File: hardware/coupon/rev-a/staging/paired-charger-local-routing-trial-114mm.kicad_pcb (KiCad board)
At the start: 6 copper layers, 114 x 32.5 mm, 483 parts, among them J1 USB4505-03-0-A, J2 S2B-PH-SM4-TB, SW1 EVQP7J01P, SW2 JS202011JCQN, U1 TLC59581RTQT, U11 SN74LVC1G04DBVR, U17 SN74LVC1G11DBVR, U2 74HC4514PW,118, U23 SN74LVC1G06DBVR, U24 SN74LVC2G17DBVR, U25 SN74LVC2G17DBVR, U29 TPS70933DBVR, U3 ESP32-S3-WROOM-1U-N16R8, U31 TUSB320LAIRWBR, U32 TS3USB31ERSER, U33 TPD4E05U06DQAR, U34 TPS3808G01DBVR, U35 MAX17048G+T10, U36 TPS631000DRLR, U37 TPS63020DSJT, U38 2.5V shunt, U39 TMP390A2DRLR, U40 SN74AUP1G125DBVR, U41 BQ24074RGTR, U42 SN74AUP1G125DBVR, U43 SN74AUP1G125DBVR, U44 TPS259474ARPWR, U45 TPS259474ARPWR, U46 TCA9517ADGKR, U47 TPS3823A-33DBVR, U48 SN74LVC1G04DSFR, U49 SN74LVC1G74RSER, U50 SN74LVC1G74RSER, U51 SN74LVC1G11DRYR, U52 SN74LVC1G08DSFR, U53 TLV6700DSER, U54 SN74LVC2G00DCUR, U55 SN74LVC2G08DCUR

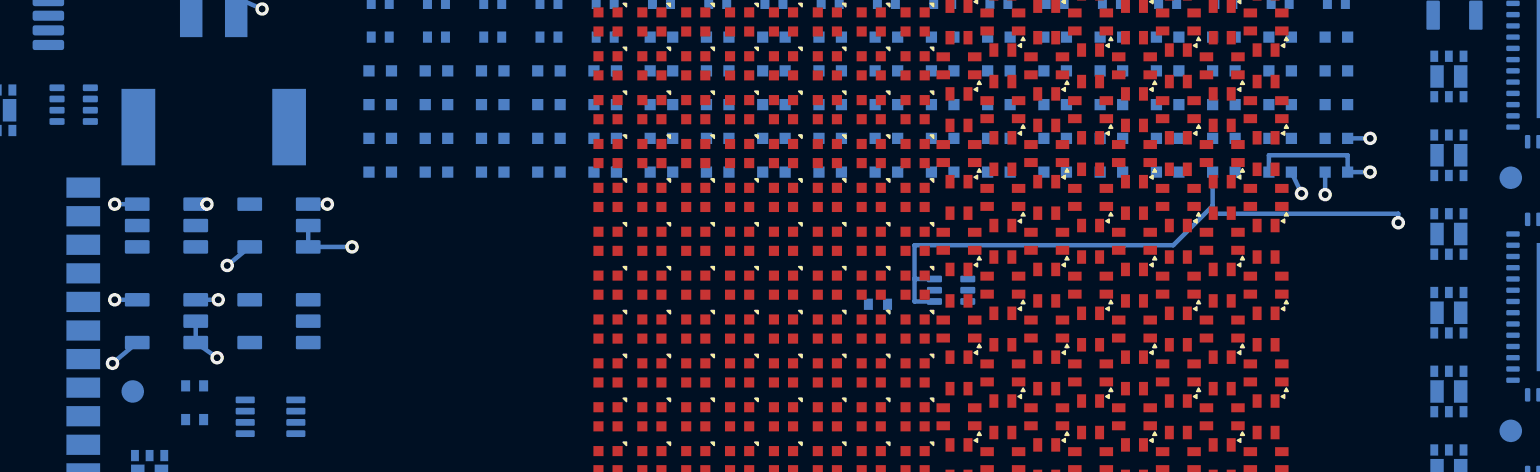
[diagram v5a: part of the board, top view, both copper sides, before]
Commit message: Join charger permission logic supply and temperature sensor returns
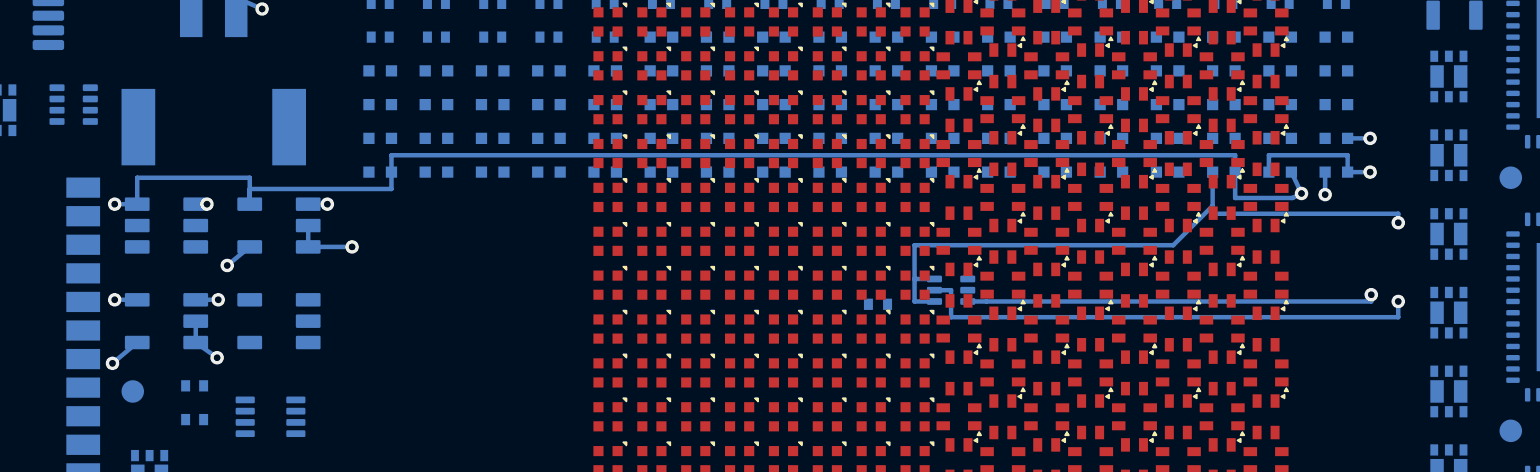
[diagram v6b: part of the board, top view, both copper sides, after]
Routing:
- net +3V3_USB: track 24.2 -> 130.5 mm, vias 6 -> 7
- net GND: track 229.2 -> 250.4 mm, vias 20 -> 21
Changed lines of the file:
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@@
+	)
+	(segment
+		(start 21.45 10.5)
+		(end 21.45 11.675)
+		(width 0.2)
+		(layer "B.Cu")
+		(net "+3V3_USB")
 	)
 	(segment
@@
 		(layer "B.Cu")
 		(net "+BAT_PROTECTED_DRAFT")
+	)
+	(segment
+		(start 26.45 10.5)
+		(end 21.45 10.5)
+		(width 0.2)
+		(layer "B.Cu")
+		(net "+3V3_USB")
+	)
+	(segment
+		(start 26.45 11)
+		(end 32.75 11)
+		(width 0.2)
+		(layer "B.Cu")
+		(net "+3V3_USB")
+	)
+	(segment
+		(start 26.45 11.675)
+		(end 26.45 10.5)
+		(width 0.2)
+		(layer "B.Cu")
+		(net "+3V3_USB")
+	)
+	(segment
+		(start 26.45 11.675)
+		(end 26.45 11)
+		(width 0.2)
+		(layer "B.Cu")
+		(net "+3V3_USB")
 	)
 	(segment
@@
 	)
 	(segment
+		(start 32.75 10.25)
+		(end 32.75 9.5)
+		(width 0.2)
+		(layer "B.Cu")
+		(net "+3V3_USB")
+	)
+	(segment
+		(start 32.75 11)
+		(end 32.75 10.25)
+		(width 0.2)
+		(layer "B.Cu")
+		(net "+3V3_USB")
+	)
+	(segment
+		(start 32.75 9.5)
+		(end 70.25 9.5)
+		(width 0.2)
+		(layer "B.Cu")
+		(net "+3V3_USB")
+	)
+	(segment
 		(start 5.3 1.4)
 		(end 6.5 1.4)
@@
 		(layer "B.Cu")
 		(net "TEMP_OK")
+	)
+	(segment
+		(start 56.885 15.5)
+		(end 57.625 15.5)
+		(width 0.2)
+		(layer "B.Cu")
+		(net "+3V3_USB")
+	)
+	(segment
+		(start 57.625 15.5)
+		(end 57.625 16.7)
+		(width 0.2)
+		(layer "B.Cu")
+		(net "+3V3_USB")
+	)
+	(segment
+		(start 57.625 16.7)
+		(end 77.5 16.7)
+		(width 0.2)
+		(layer "B.Cu")
+		(net "+3V3_USB")
+	)
+	(segment
+		(start 58.365 16)
+		(end 59.2 16)
+		(width 0.2)
+		(layer "B.Cu")
+		(net "GND")
+	)
+	(segment
+		(start 59.2 16)
+		(end 76.3 16)
+		(width 0.2)
+		(layer "B.Cu")
+		(net "GND")
 	)
 	(segment
@@
 	)
 	(segment
+		(start 70.25 10.25)
+		(end 70.25 11.4)
+		(width 0.2)
+		(layer "B.Cu")
+		(net "+3V3_USB")
+	)
+	(segment
+		(start 70.25 11.4)
+		(end 72.8 11.4)
+		(width 0.2)
+		(layer "B.Cu")
+		(net "+3V3_USB")
+	)
+	(segment
+		(start 70.25 9.5)
+		(end 70.25 10.25)
+		(width 0.2)
+		(layer "B.Cu")
+		(net "+3V3_USB")
+	)
+	(segment
 		(start 71.75 10.25)
 		(end 71.75 9.5)
@@
 	)
 	(segment
+		(start 72.8 11.4)
+		(end 73.2 11.2)
+		(width 0.2)
+		(layer "B.Cu")
+		(net "+3V3_USB")
+	)
+	(segment
 		(start 73.2 11.2)
 		(end 76.25 8.75)
@@
 	)
 	(segment
+		(start 76.25 8.75)
+		(end 91.2 6.625)
+		(width 0.2)
+		(layer "In2.Cu")
+		(net "+3V3_USB")
+	)
+	(segment
+		(start 76.3 15.7)
+		(end 76.3 18.73)
+		(width 0.2)
+		(layer "In2.Cu")
+		(net "GND")
+	)
+	(segment
+		(start 76.3 16)
+		(end 76.3 15.7)
+		(width 0.2)
+		(layer "B.Cu")
+		(net "GND")
+	)
+	(segment
 		(start 77.5 12.1)
 		(end 77.5 12.5)
@@
 	)
 	(segment
+		(start 77.5 16)
+		(end 78.5 16)
+		(width 0.2)
+		(layer "In2.Cu")
+		(net "+3V3_USB")
+	)
+	(segment
+		(start 77.5 16.7)
+		(end 77.5 16)
+		(width 0.2)
+		(layer "B.Cu")
+		(net "+3V3_USB")
+	)
+	(segment
 		(start 77.5 9.5)
 		(end 77.5 12.5)
@@
 	)
 	(segment
+		(start 78.5 16)
+		(end 78.5 8.75)
+		(width 0.2)
+		(layer "In2.Cu")
+		(net "+3V3_USB")
+	)
+	(segment
+		(start 78.5 8.75)
+		(end 76.25 8.75)
+		(width 0.2)
+		(layer "In2.Cu")
+		(net "+3V3_USB")
+	)
+	(segment
 		(start 90 14.175)
 		(end 91.2 14.175)
@@
 	)
 	(via
+		(at 76.3 15.7)
+		(size 0.6)
+		(drill 0.3)
+		(layers "F.Cu" "B.Cu")
+		(net "GND")
+	)
+	(via
 		(at 77.5 12.5)
 		(size 0.6)
@@
 	)
 	(via
+		(at 77.5 16)
+		(size 0.6)
+		(drill 0.3)
+		(layers "F.Cu" "B.Cu")
+		(net "+3V3_USB")
+	)
+	(via

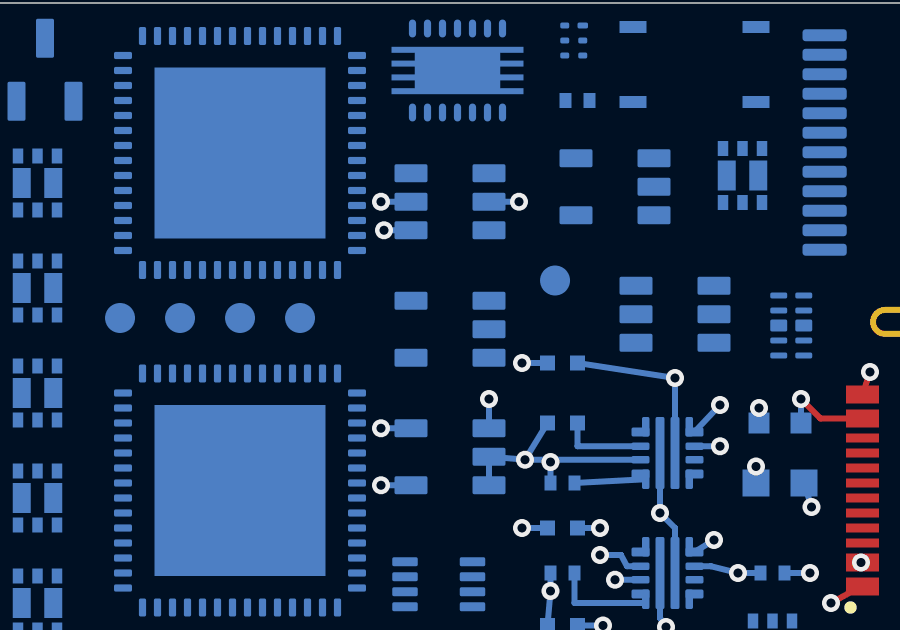
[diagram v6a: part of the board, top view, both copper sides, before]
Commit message: Route USB logic LDO output and return on study board
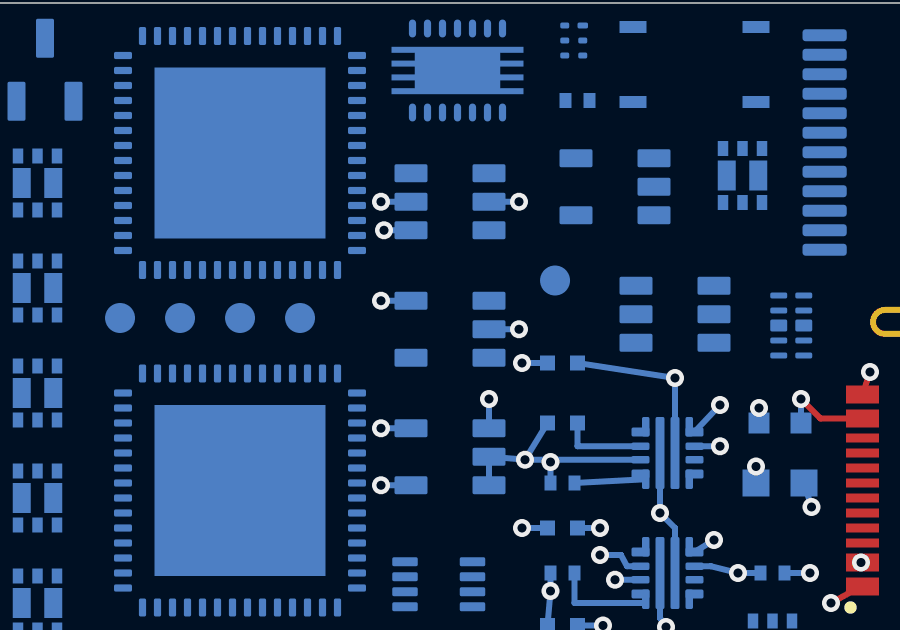
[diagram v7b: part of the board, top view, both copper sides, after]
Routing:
- net GND: track 250.4 -> 253.2 mm, vias 21 -> 22
- net +3V3_USB: track 130.5 -> 132.7 mm, vias 7 -> 8
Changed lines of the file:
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@@
+	)
+	(segment
+		(start 91.2 9.925)
+		(end 90 9.925)
+		(width 0.2)
+		(layer "In2.Cu")
+		(net "+3V3_USB")
 	)
 	(segment
@@
 	)
 	(segment
+		(start 92.2 9.925)
+		(end 91.2 9.925)
+		(width 0.2)
+		(layer "B.Cu")
+		(net "+3V3_USB")
+	)
+	(segment
 		(start 93 14.3)
 		(end 101 14.3)
@@
 	)
 	(segment
+		(start 94.8 10.875)
+		(end 95.8 10.875)
+		(width 0.2)
+		(layer "B.Cu")
+		(net "GND")
+	)
+	(segment
 		(start 94.8 14.175)
 		(end 94.8 13.2)
@@
 	)
 	(segment
+		(start 95.8 10.875)
+		(end 94 10.875)
+		(width 0.2)
+		(layer "In2.Cu")
+		(net "GND")
+	)
+	(segment
 		(start 95.8 6.625)
 		(end 94 6.625)
@@
 	)
 	(via
+		(at 91.2 9.925)
+		(size 0.6)
+		(drill 0.3)
+		(layers "F.Cu" "B.Cu")
+		(net "+3V3_USB")
+	)
+	(via
 		(at 91.3 7.575)
 		(size 0.6)
@@
 	)
 	(via
+		(at 95.8 10.875)
+		(size 0.6)
+		(drill 0.3)
+		(layers "F.Cu" "B.Cu")
+		(net "GND")
+	)
+	(via

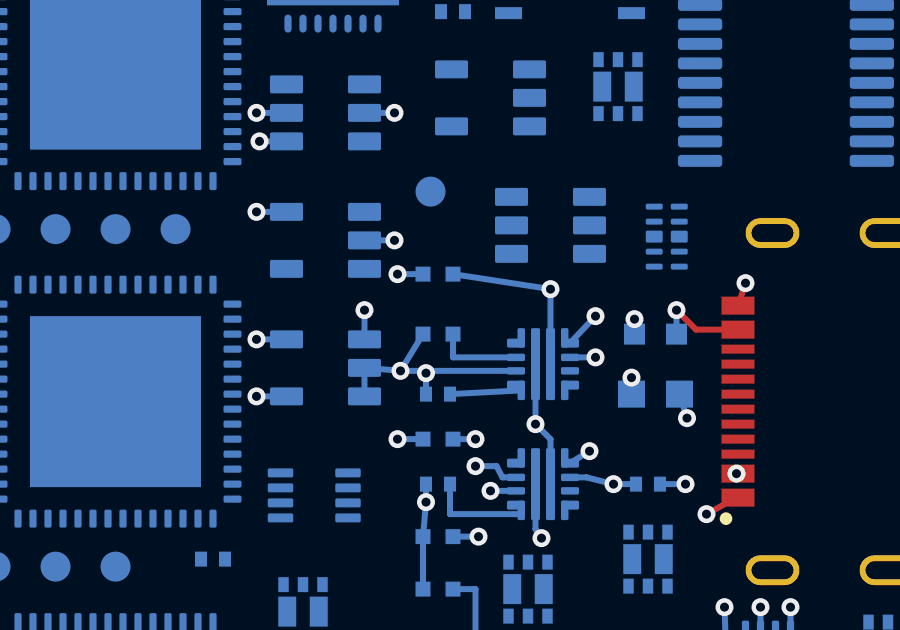
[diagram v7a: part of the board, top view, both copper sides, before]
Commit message: Route protected USB rail to logic LDO input
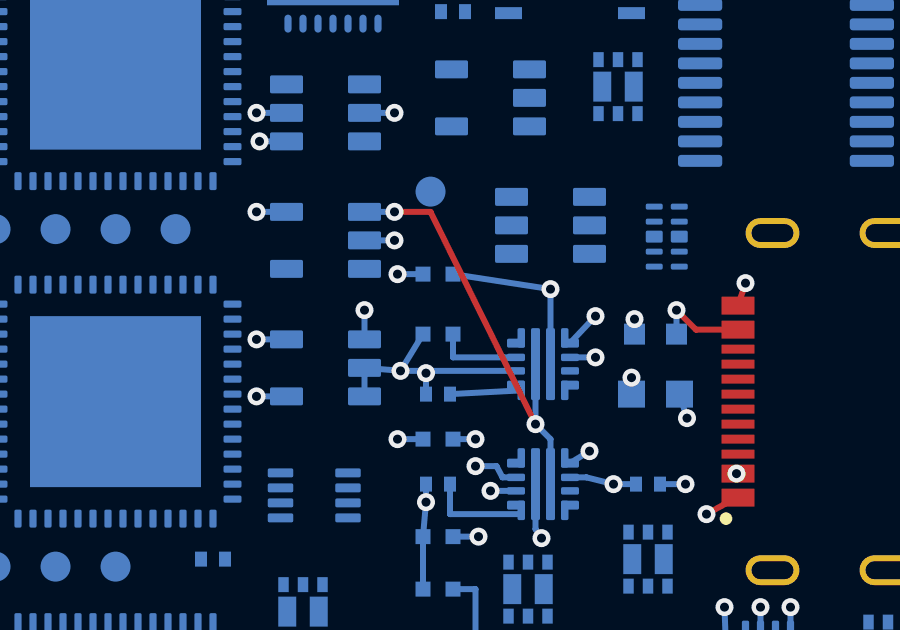
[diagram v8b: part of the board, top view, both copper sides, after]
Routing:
- net +5V_USB: track 10.2 -> 20.3 mm, vias 2 -> 3
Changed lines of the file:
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@@
+	)
+	(segment
+		(start 94.8 9.925)
+		(end 95.8 9.925)
+		(width 0.2)
+		(layer "B.Cu")
+		(net "+5V_USB")
 	)
 	(segment
@@
 	)
 	(segment
+		(start 95.8 9.925)
+		(end 97 9.925)
+		(width 0.2)
+		(layer "F.Cu")
+		(net "+5V_USB")
+	)
+	(segment
 		(start 95.9 12)
 		(end 100 11.5)
@@
 	)
 	(segment
+		(start 97 9.925)
+		(end 100.5 17)
+		(width 0.2)
+		(layer "F.Cu")
+		(net "+5V_USB")
+	)
+	(segment
 		(start 97.65 16)
 		(end 100.025 15.875)
@@
 	)
 	(via
+		(at 95.8 9.925)
+		(size 0.6)
+		(drill 0.3)
+		(layers "F.Cu" "B.Cu")
+		(net "+5V_USB")
+	)
+	(via
